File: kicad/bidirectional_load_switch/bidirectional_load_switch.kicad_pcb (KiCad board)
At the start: 2 copper layers, 176.5 x 67.5 mm, 166 parts, among them J102 Conn_01x02_Socket, J103 Conn_01x09_Socket, J104 Conn_01x02_Socket, J105 Conn_01x02_Socket, J106 Conn_01x02_Socket, J107 AVR-ISP-6

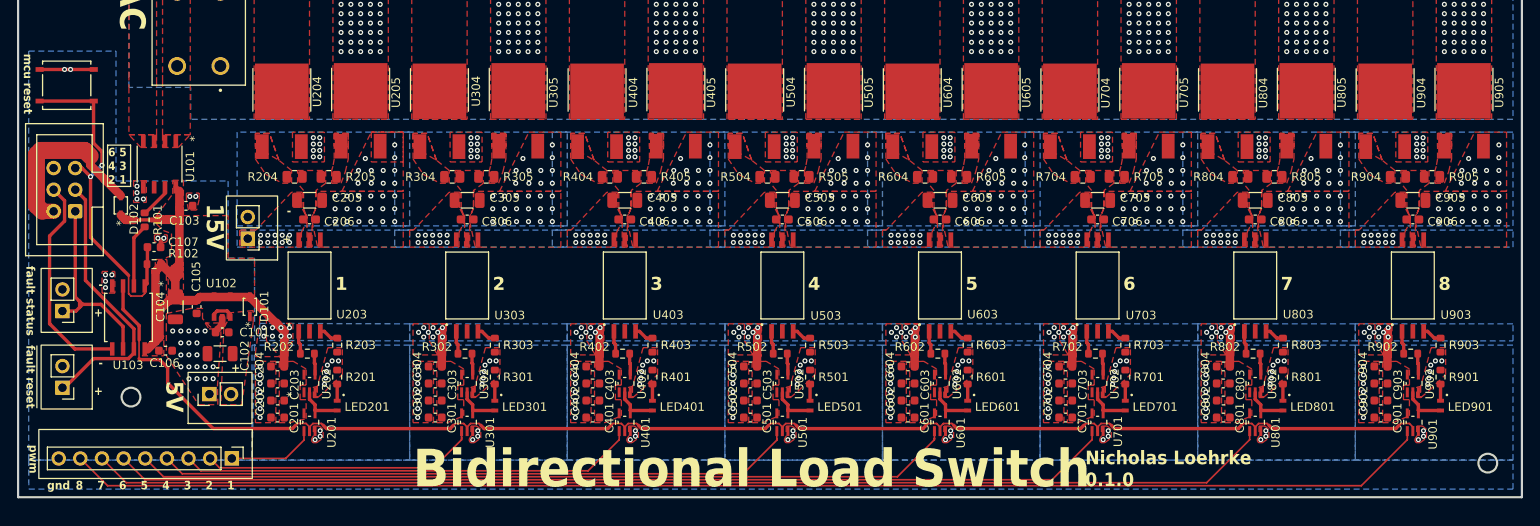
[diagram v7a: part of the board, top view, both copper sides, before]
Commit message: removed redundant buffer
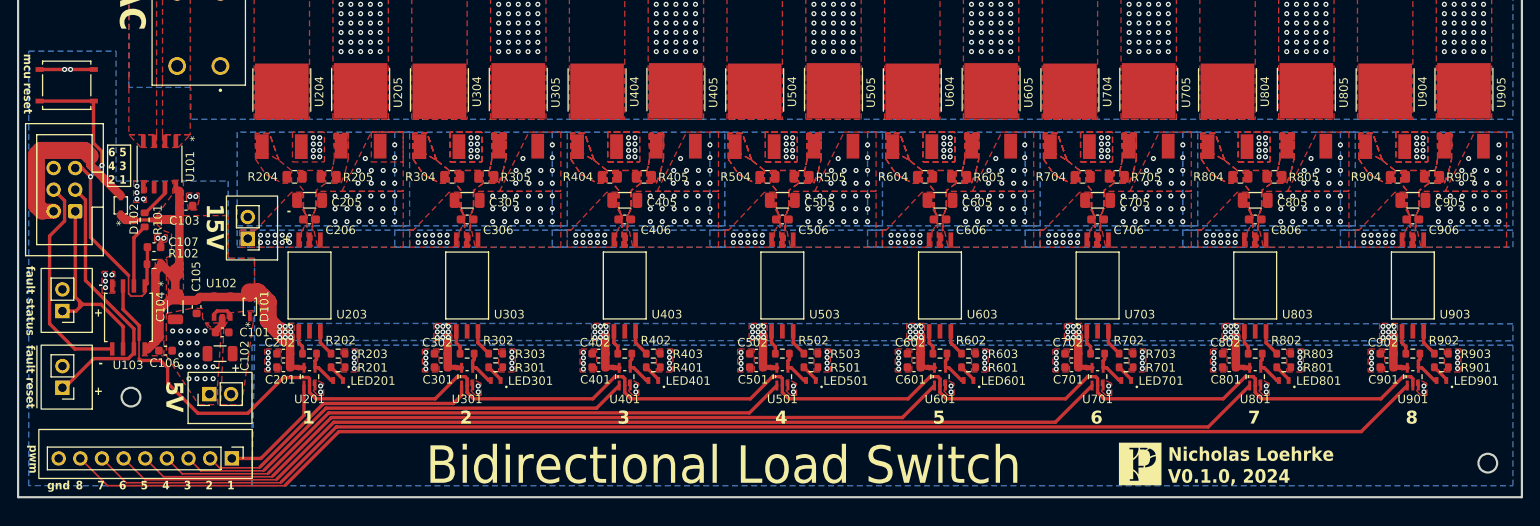
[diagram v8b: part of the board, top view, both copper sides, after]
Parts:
- removed C203, C303, C403, C503, C603, C703, C803, C903: 1u, Capacitor_SMD:C_0603_1608Metric
- removed C204, C304, C404, C504, C604, C704, C804, C904: 100n, Capacitor_SMD:C_0603_1608Metric
- removed U202, U302, U402, U502, U602, U702, U802, U902: ~, buffer_SN74LVC1G17DCKR:DCK5
- added G***: LOGO, platteville_logo:5x5_positive, F.Cu at (193.8, 124.8)
- moved C201 5.94 mm to (93.2, 113.4)
- moved C301 5.94 mm to (111.8, 113.4)
- moved C401 5.94 mm to (130.2, 113.4)
- moved C501 5.94 mm to (148.8, 113.4)
- moved C601 5.94 mm to (167.2, 113.4)
- moved C701 5.94 mm to (185.8, 113.4)
- moved C801 5.94 mm to (204.2, 113.4)
- moved C901 5.94 mm to (222.8, 113.4)
- moved C202 5.54 mm to (93.2, 111.8)
- moved C302 5.54 mm to (111.8, 111.8)
- moved C402 5.54 mm to (130.2, 111.8)
- moved C502 5.54 mm to (148.8, 111.8)
- moved C602 5.54 mm to (167.2, 111.8)
- moved C702 5.54 mm to (185.8, 111.8)
- moved C802 5.54 mm to (204.2, 111.8)
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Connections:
- R202 pad 1: Net-(U202-Y) -> Net-(U201-Y)
- R302 pad 1: Net-(U302-Y) -> Net-(U301-Y)
- R402 pad 1: Net-(U402-Y) -> Net-(U401-Y)
- R502 pad 1: Net-(U502-Y) -> Net-(U501-Y)
- R602 pad 1: Net-(U602-Y) -> Net-(U601-Y)
- R702 pad 1: Net-(U702-Y) -> Net-(U701-Y)
- R802 pad 1: Net-(U802-Y) -> Net-(U801-Y)
- R902 pad 1: Net-(U902-Y) -> Net-(U901-Y)
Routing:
- net ~{fault}: track 173.6 -> 186.9 mm
- net 3V3: track 103.0 -> 107.3 mm, vias 71 -> 72
- net PWM1_in: track 10.4 -> 14.1 mm
- net Net-(U202-Y): track 2.49 -> 0.00 mm
- net Net-(U302-Y): track 2.49 -> 0.00 mm
- net Net-(U902-Y): track 2.49 -> 0.00 mm
- net Net-(U802-Y): track 2.49 -> 0.00 mm
- net Net-(U702-Y): track 2.49 -> 0.00 mm
- net Net-(U602-Y): track 2.49 -> 0.00 mm
- net Net-(U502-Y): track 2.49 -> 0.00 mm
- net Net-(U402-Y): track 2.49 -> 0.00 mm
- net PWM2_in: track 32.3 -> 34.6 mm
- net PWM7_in: track 139.0 -> 140.6 mm
- net PWM6_in: track 117.7 -> 119.3 mm
- net PWM3_in: track 53.7 -> 55.3 mm
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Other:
- board text added: "Nicholas Loehrke V0.1.0, 2024"
- board text removed: "Nicholas Loehrke 0.1.0"
